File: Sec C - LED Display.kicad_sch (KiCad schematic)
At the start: 16 parts

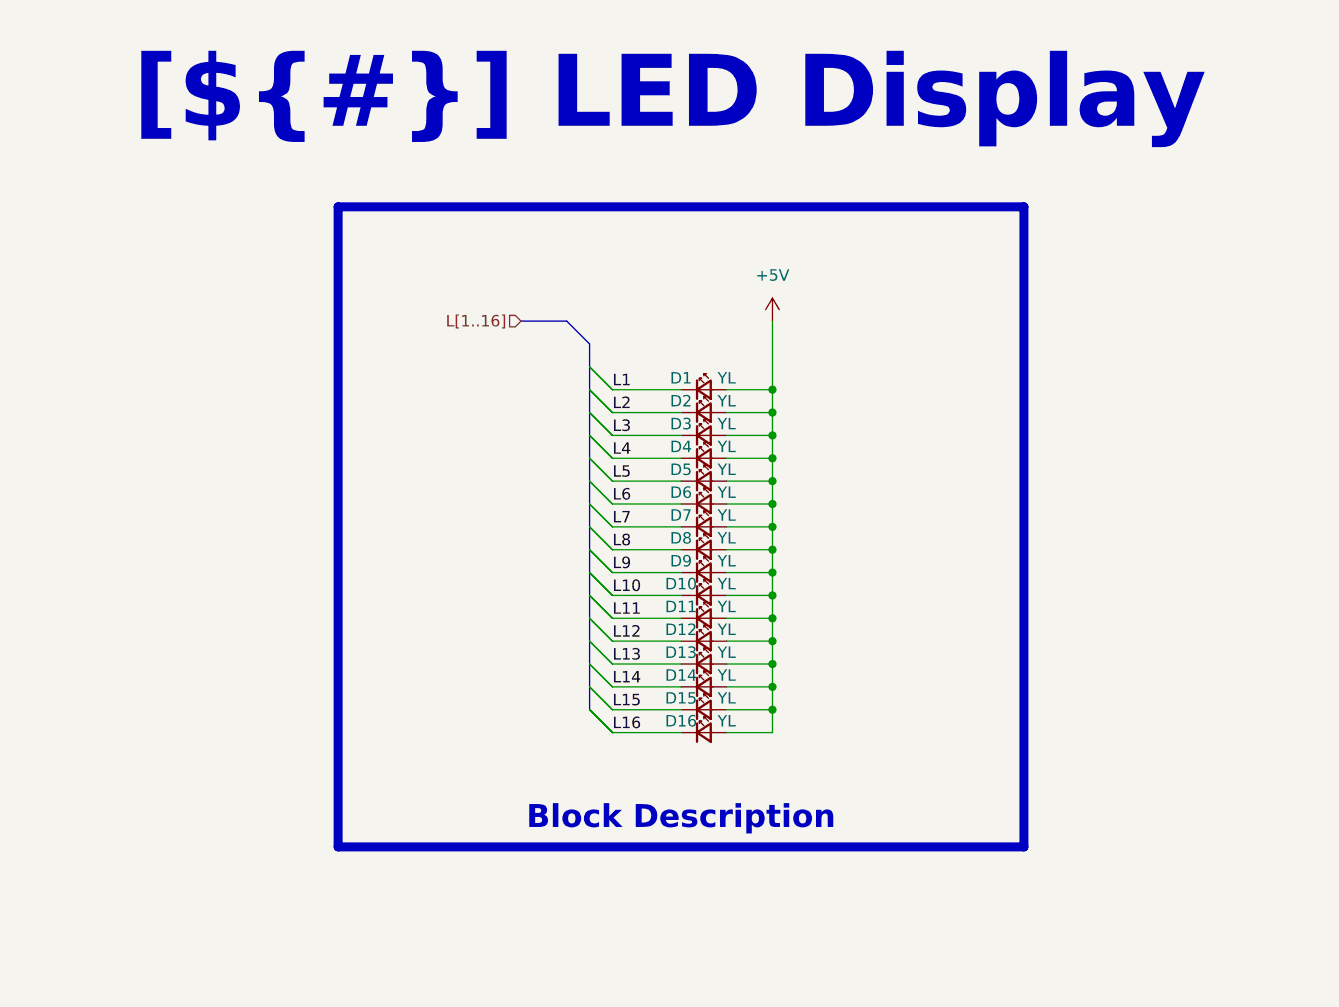
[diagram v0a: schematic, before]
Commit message: documentation update / block diagram
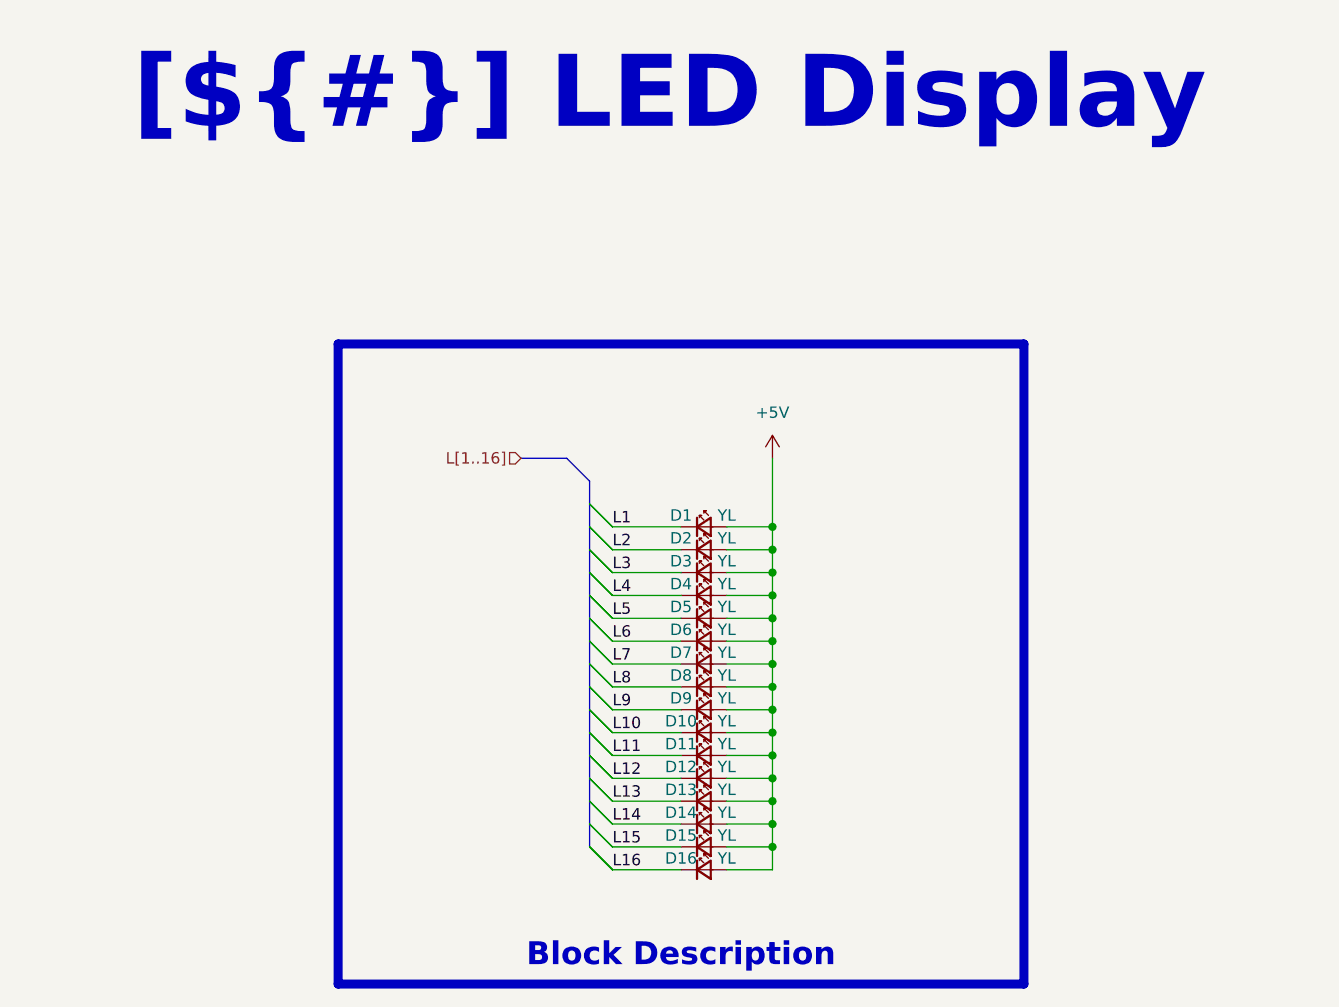
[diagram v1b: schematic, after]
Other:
- moved on the sheet: D1, D10, D11, D12, D13, D14, D15, D16, D2, D3, D4, D5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
